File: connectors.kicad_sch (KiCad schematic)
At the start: 13 parts, among them J1 USB-C_DX07S024JJ2, J2 PCIe_x4_Conn_EdgeMount_Open, J3 Molex_Nano-Fit-1053xx_xx02-ho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

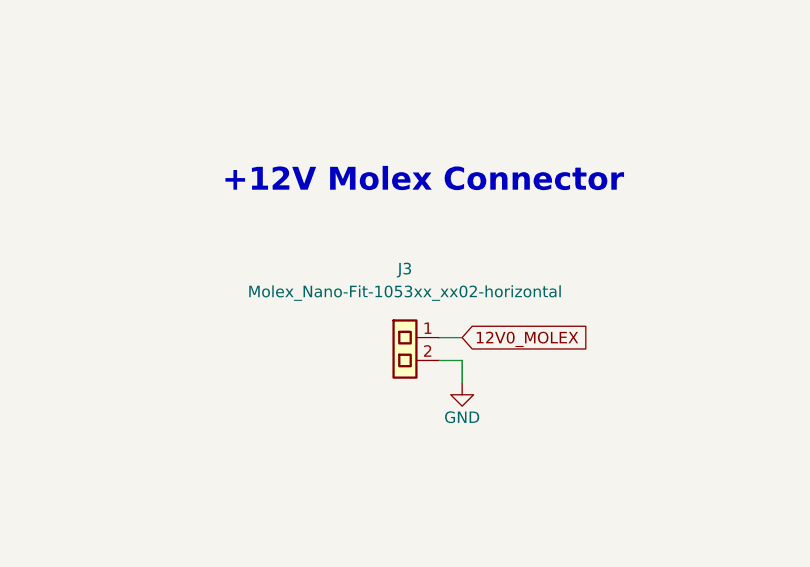
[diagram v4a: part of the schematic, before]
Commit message: Standardize all footprints on PCB
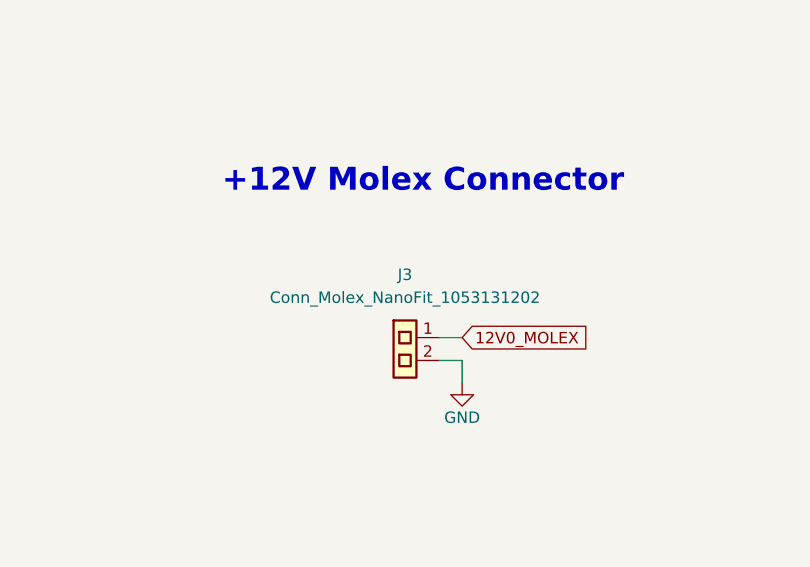
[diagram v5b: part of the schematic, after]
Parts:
- removed J3: Molex_Nano-Fit-1053xx_xx02-horizontal, antmicro-footprints:Molex_Nano-Fit_1053xx-xx02_1x02_P2.50mm_Horizontal, symbol antmicroRectangularConnectorsHeadersFemalePins:Molex_Nano-Fit-1053xx_xx02-horiz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
- added J3: Conn_Molex_NanoFit_1053131202, antmicro-footprints:Conn_Molex_NanoFit_1053131202, symbol antmicroRectangularConnectorsHeadersFemalePins:Conn_Molex_NanoFit_1053131202
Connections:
- net 12V0_MOLEX: now also J3.1
- net GND: now also J3.2
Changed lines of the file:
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@@
+    (pin "2")
+  )
+  (symbol (lib_id "antmicroRectangularConnectorsHeadersFemalePins:Conn_Molex_NanoFit_1053131202") (at 151.765 192.405 0) (unit 1)
+    (in_bom yes) (on_board yes) (fields_autoplaced)
+    (property "Reference" "J3" (id 0) (at 147.955 185.42 0)
+      (effects (font (size 1.27 1.27) (thickness 0.15)))
+    )
+    (property "Value" "Conn_Molex_NanoFit_1053131202" (id 1) (at 147.955 187.96 0)
+      (effects (font (size 1.27 1.27) (thickness 0.15)))
+    )
+    (property "Footprint" "antmicro-footprints:Conn_Molex_NanoFit_1053131202" (id 2) (at 172.085 202.565 0)
+      (effects (font (size 1.27 1.27) (thickness 0.15)) (justify left bottom) hide)
+    )
+    (property "Datasheet" "https://www.molex.com/molex/products/part-detail/pcb_headers/1053131202" (id 3) (at 172.085 205.105 0)
+      (effects (font (size 1.27 1.27) (thickness 0.15)) (justify left bottom) hide)
+    )
+    (property "Manufacturer" "Molex" (id 4) (at 172.085 207.645 0)
+      (effects (font (size 1.27 1.27) (thickness 0.15)) (justify left bottom) hide)
+    )
+    (property "MPN" "1053131202" (id 5) (at 172.085 210.185 0)
+      (effects (font (size 1.27 1.27) (thickness 0.15)) (justify left bottom) hide)
+    )
+    (property "Author" "Antmicro" (id 6) (at 172.085 212.725 0)
+      (effects (font (size 1.27 1.27) (thickness 0.15)) (justify left bottom) hide)
+    )
+    (property "License" "Apache-2.0" (id 7) (at 172.085 215.265 0)
+      (effects (font (size 1.27 1.27) (thickness 0.15)) (justify left bottom) hide)
+    )
+    (pin "1")
     (pin "2")
   )
@@
     (pin "1")
   )
-  (symbol (lib_id "antmicroRectangularConnectorsHeadersFemalePins:Molex_Nano-Fit-1053xx_xx02-horizontal") (at 151.765 192.405 0) (unit 1)
-    (in_bom yes) (on_board yes) (fields_autoplaced)
-    (property "Reference" "J3" (id 0) (at 147.955 184.785 0))
-    (property "Value" "Molex_Nano-Fit-1053xx_xx02-horizontal" (id 1) (at 147.955 187.325 0))
-    (property "Footprint" "antmicro-footprints:Molex_Nano-Fit_1053xx-xx02_1x02_P2.50mm_Horizontal" (id 2) (at 147.32 200.66 0)
-      (effects (font (size 1.27 1.27)) hide)
-    )
-    (property "Datasheet" "https://www.molex.com/molex/products/part-detail/pcb_headers/1053131202" (id 3) (at 151.765 192.405 0)
-      (effects (font (size 1.27 1.27)) hide)
-    )
-    (property "Manufacturer" "Molex" (id 4) (at 150.495 205.74 0)
-      (effects (font (size 1.27 1.27)) hide)
-    )
-    (property "MPN" "1053131202" (id 5) (at 148.59 203.835 0)
-      (effects (font (size 1.27 1.27)) hide)
-    )
-    (property "Author" "Antmicro" (id 6) (at 172.085 212.725 0)
-      (effects (font (size 1.27 1.27) (thickness 0.15)) (justify left bottom) hide)
-    )
-    (property "License" "Apache-2.0" (id 7) (at 172.085 215.265 0)
-      (effects (font (size 1.27 1.27) (thickness 0.15)) (justify left bottom) hide)
-    )
-    (pin "1")
-    (pin "2")
-  )
   (symbol (lib_id "antmicropower:GND") (at 205.74 298.45 0) (unit 1)

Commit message: Update naming convention
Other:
- title: (none) -> Thunderbolt PCIe Adaper
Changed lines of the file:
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@@
   (paper "A3" portrait)
   (title_block
-    (date "2023-05-09")
+    (title "Thunderbolt PCIe Adaper")
+    (date "2023-06-05")
     (rev "1.0.0")
     (comment 1 "www.antmicro.com")

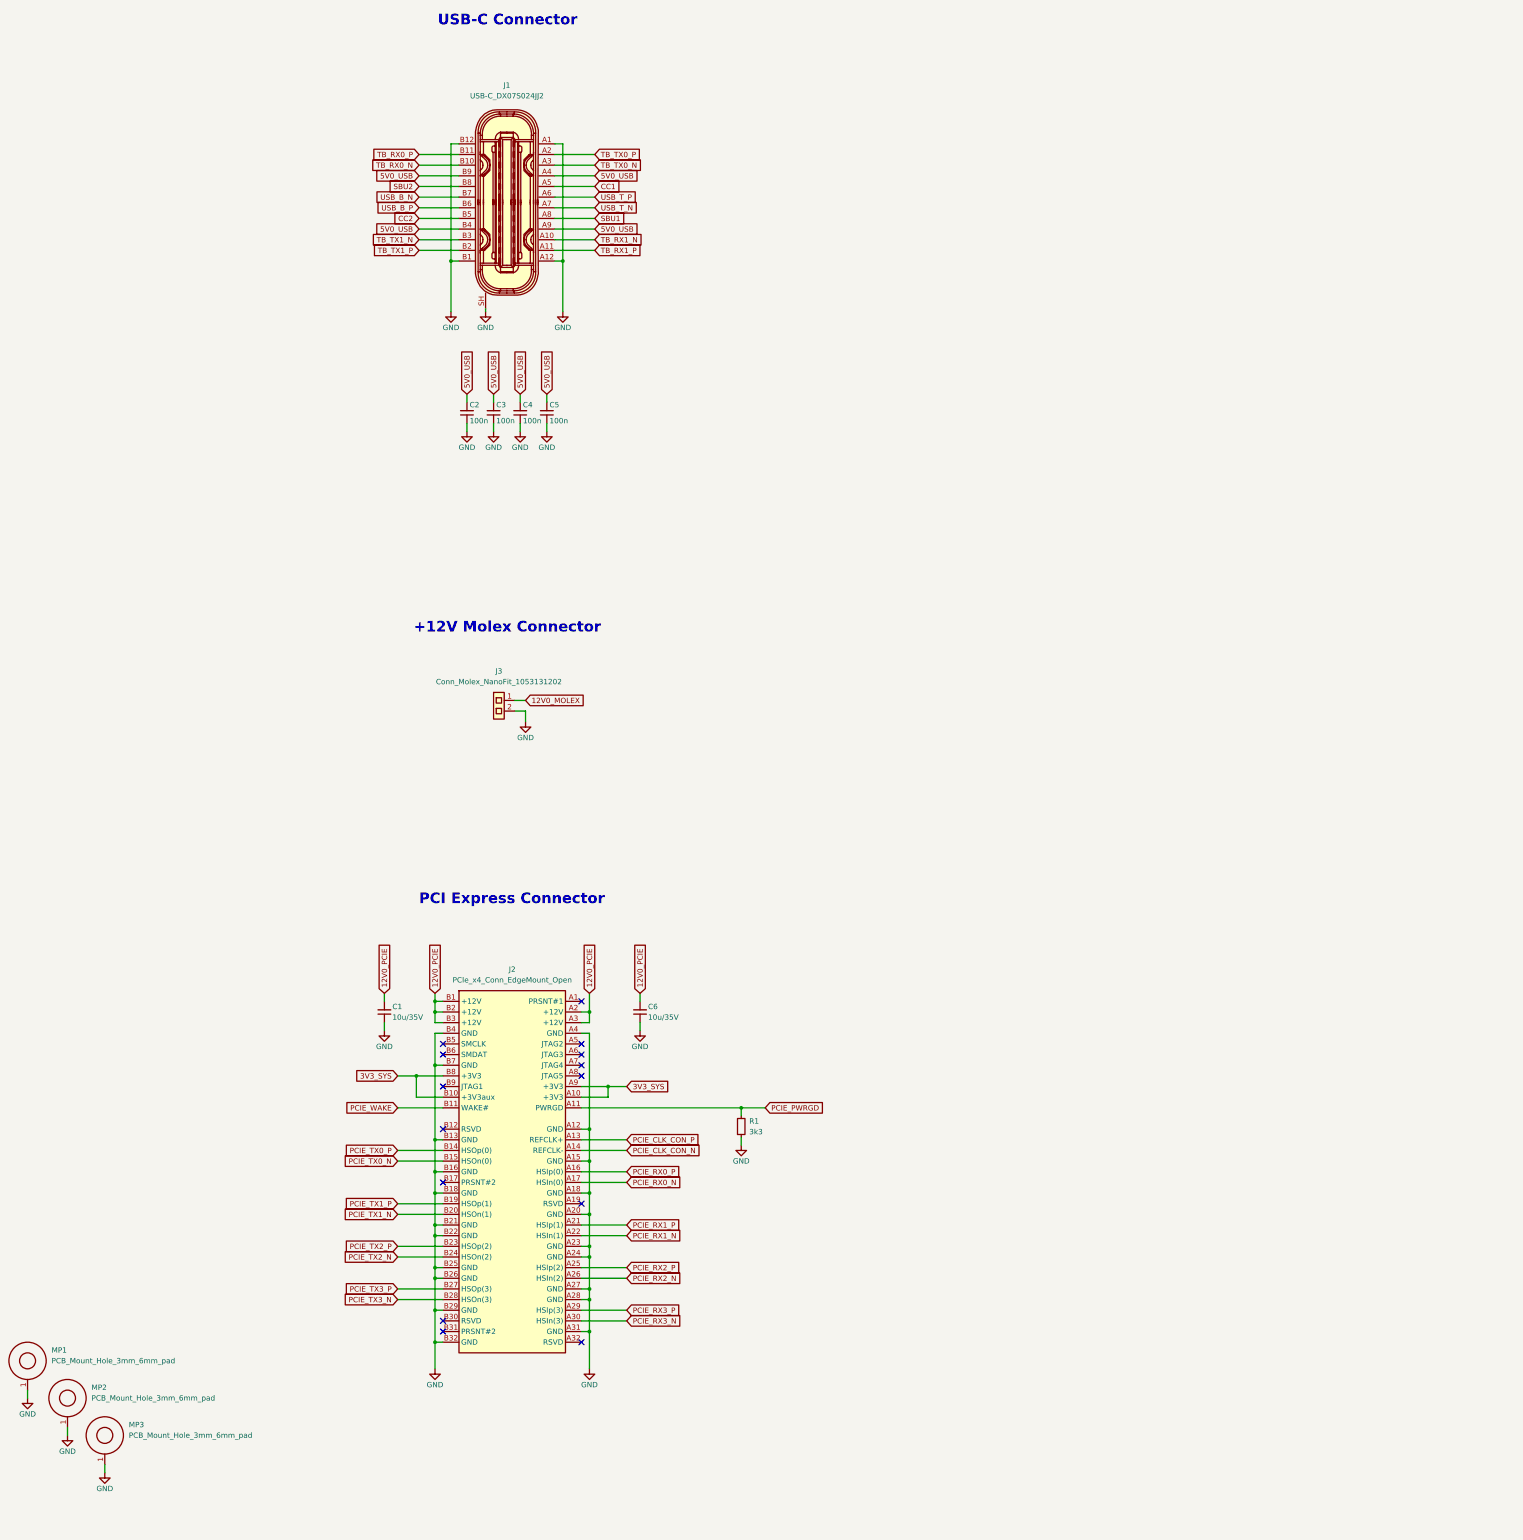
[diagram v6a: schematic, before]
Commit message: Change symbol of U4, redraw schematic to use landscape orientation
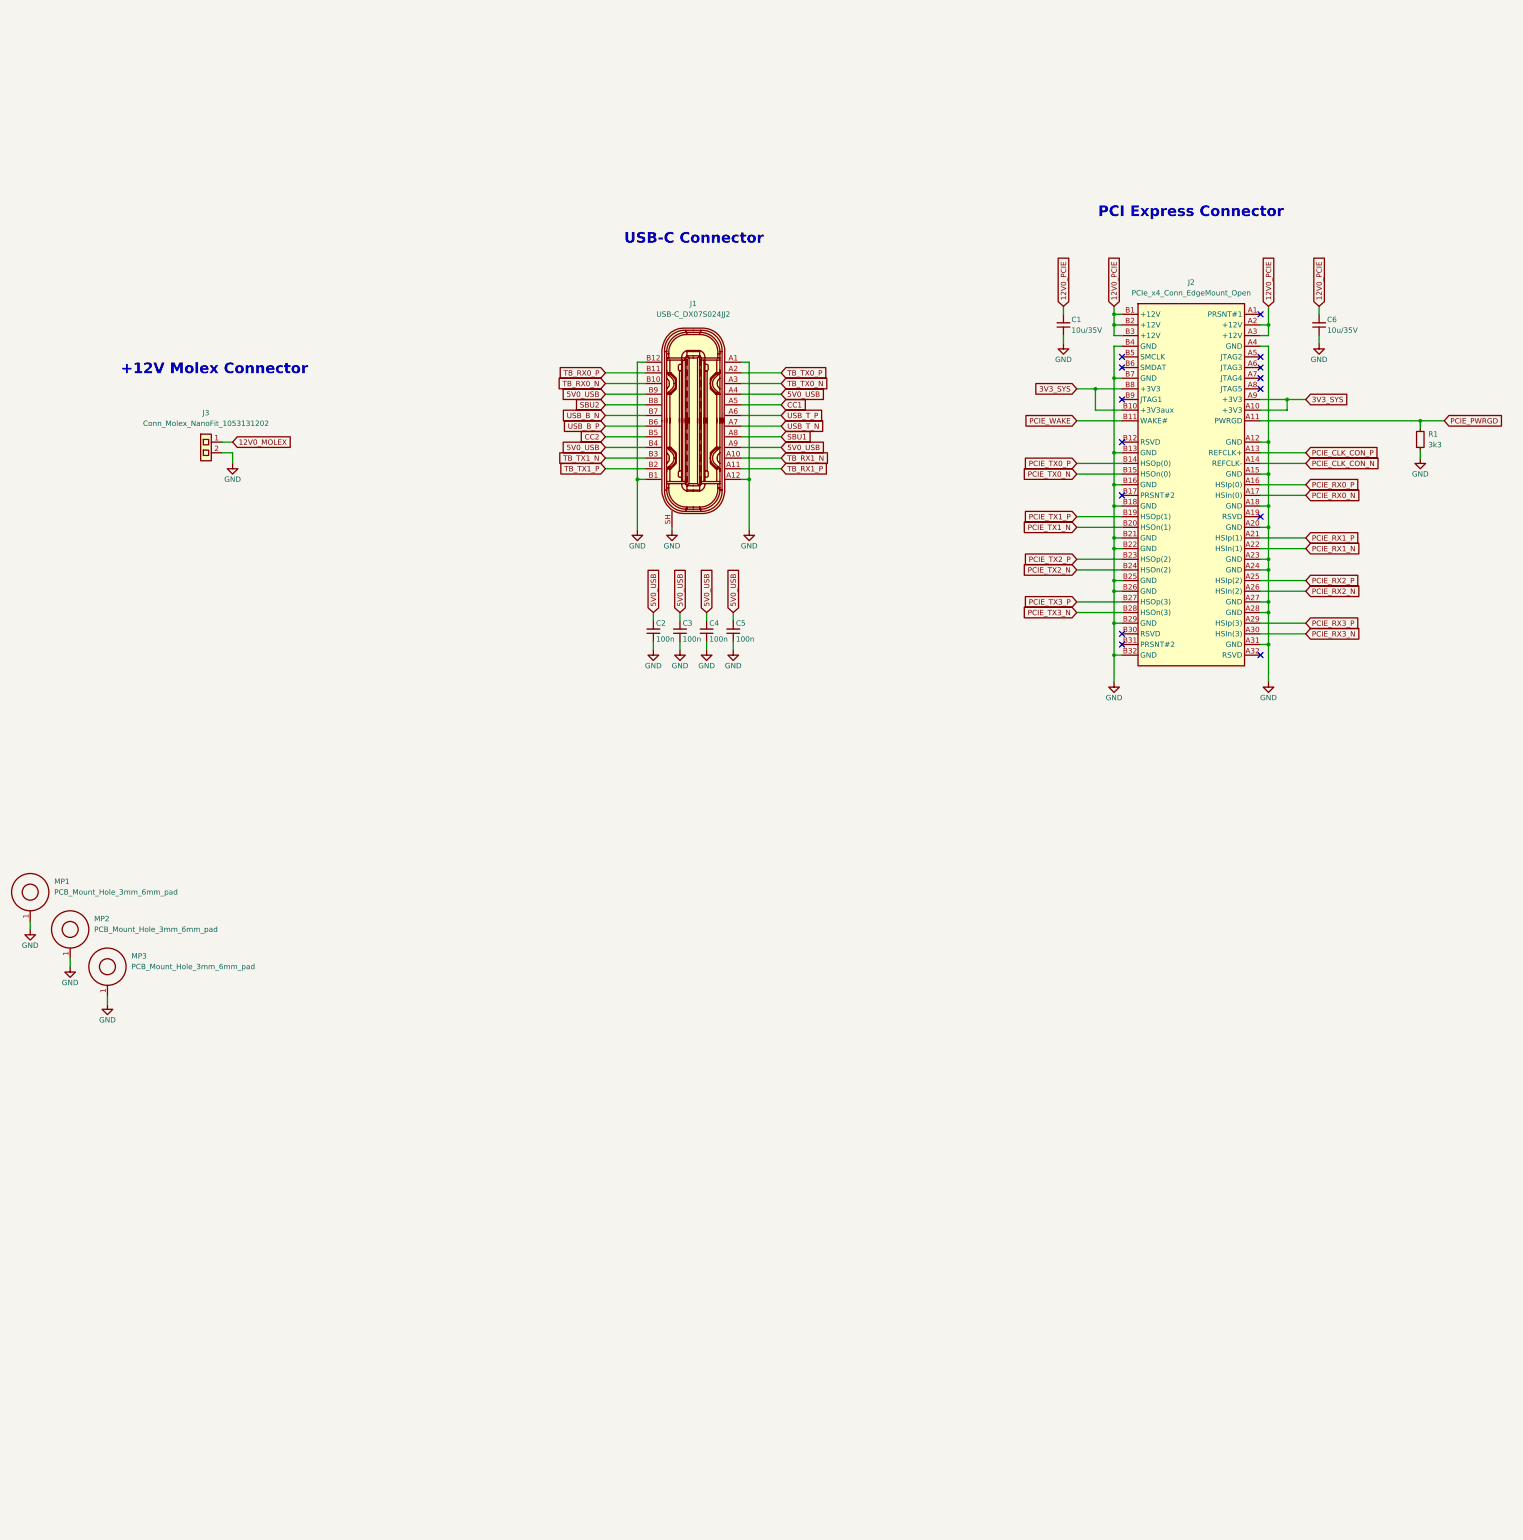
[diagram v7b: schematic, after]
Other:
- moved on the sheet: C1, C2, C3, C4, C5, C6, J1, J2, J3, MP1, MP2, MP3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

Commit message: Generate library of local components
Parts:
- C1, C6: footprint antmicro-footprints:C_0805_2012Metric -> thunderbolt-pcie-adapter-footprints:C_0805_2012Metric; symbol antmicroCapacitorsmisc:C_10u_0805_35V -> thunderbolt-pcie-adapter:C_10u_0805_35V
- C2, C3, C4, C5: footprint antmicro-footprints:C_0402_1005Metric -> thunderbolt-pcie-adapter-footprints:C_0402_1005Metric; symbol antmicroCapacitors0402:C_100n_0402 -> thunderbolt-pcie-adapter:C_100n_0402
- J1: footprint antmicro-footprints:USB-3.1-Gen2_Type-C_JAE_DX07S024JJ2_Horizontal -> thunderbolt-pcie-adapter-footprints:USB-3.1-Gen2_Type-C_JAE_DX07S024JJ2_Horizontal; symbol antmicroUSBDVIHDMIConnectors:USB-C_DX07S024JJ2 -> thunderbolt-pcie-adapter:USB-C_DX07S024JJ2
- J2: footprint antmicro-footprints:PCIE_TE_2-2387405-2 -> thunderbolt-pcie-adapter-footprints:PCIE_TE_2-2387405-2; symbol antmicroPciConnectors:PCIe_x4_Conn_EdgeMount_Open -> thunderbolt-pcie-adapter:PCIe_x4_Conn_EdgeMount_Open
- J3: footprint antmicro-footprints:Conn_Molex_NanoFit_1053131202 -> thunderbolt-pcie-adapter-footprints:Conn_Molex_NanoFit_1053131202; symbol antmicroRectangularConnectorsHeadersFemalePins:Conn_Molex_NanoFit_1053131202 -> thunderbolt-pcie-adapter:Conn_Molex_NanoFit_1053131202
- MP1, MP2, MP3: footprint antmicro-footprints:mounting-hole-3.2mm -> thunderbolt-pcie-adapter-footprints:mounting-hole-3.2mm; symbol antmicroMechanicalParts:PCB_Mount_Hole_3mm_6mm_pad -> thunderbolt-pcie-adapter:PCB_Mount_Hole_3mm_6mm_pad
- R1: footprint antmicro-footprints:R_0402_1005Metric -> thunderbolt-pcie-adapter-footprints:R_0402_1005Metric; symbol antmicroResistors0402:R_3k3_0402 -> thunderbolt-pcie-adapter:R_3k3_0402
